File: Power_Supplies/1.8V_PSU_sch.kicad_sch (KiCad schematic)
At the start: 8 parts, among them U2 TPS62822DLC

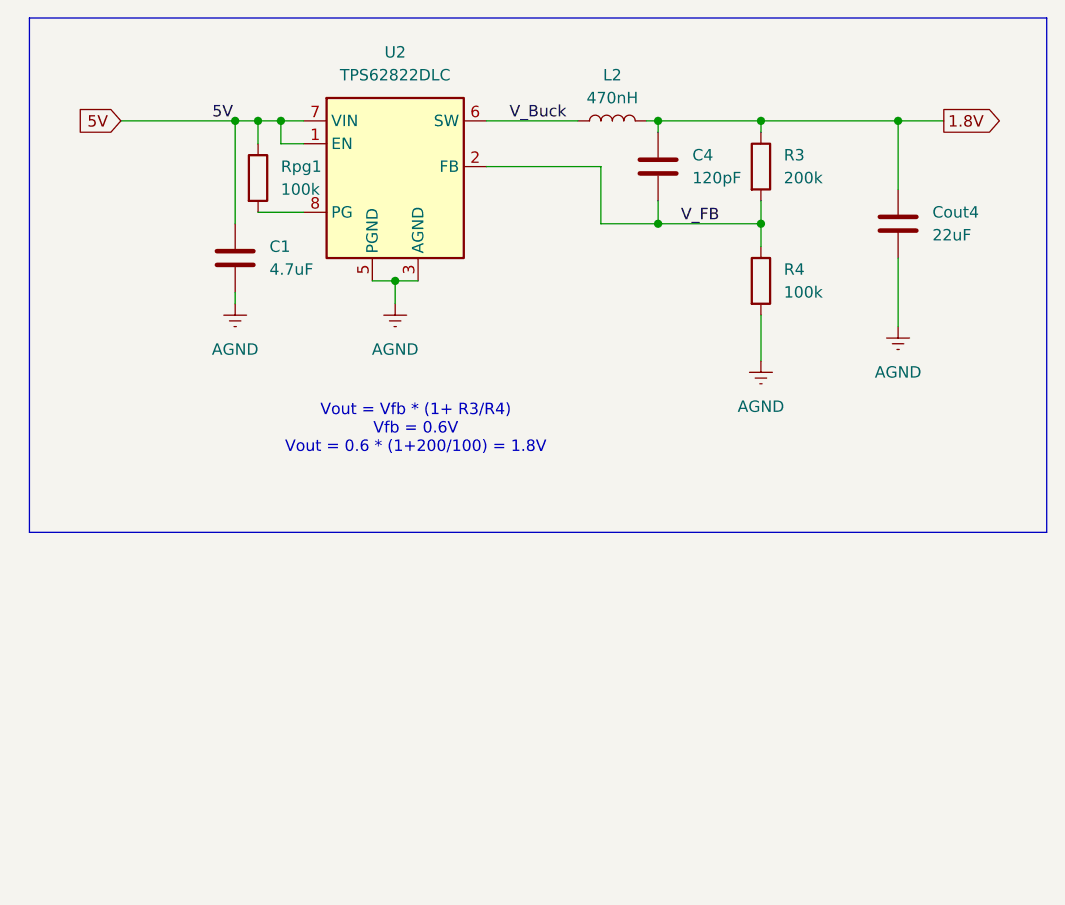
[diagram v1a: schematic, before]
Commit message: Added 3.3V/1.8V LDO, clock IC
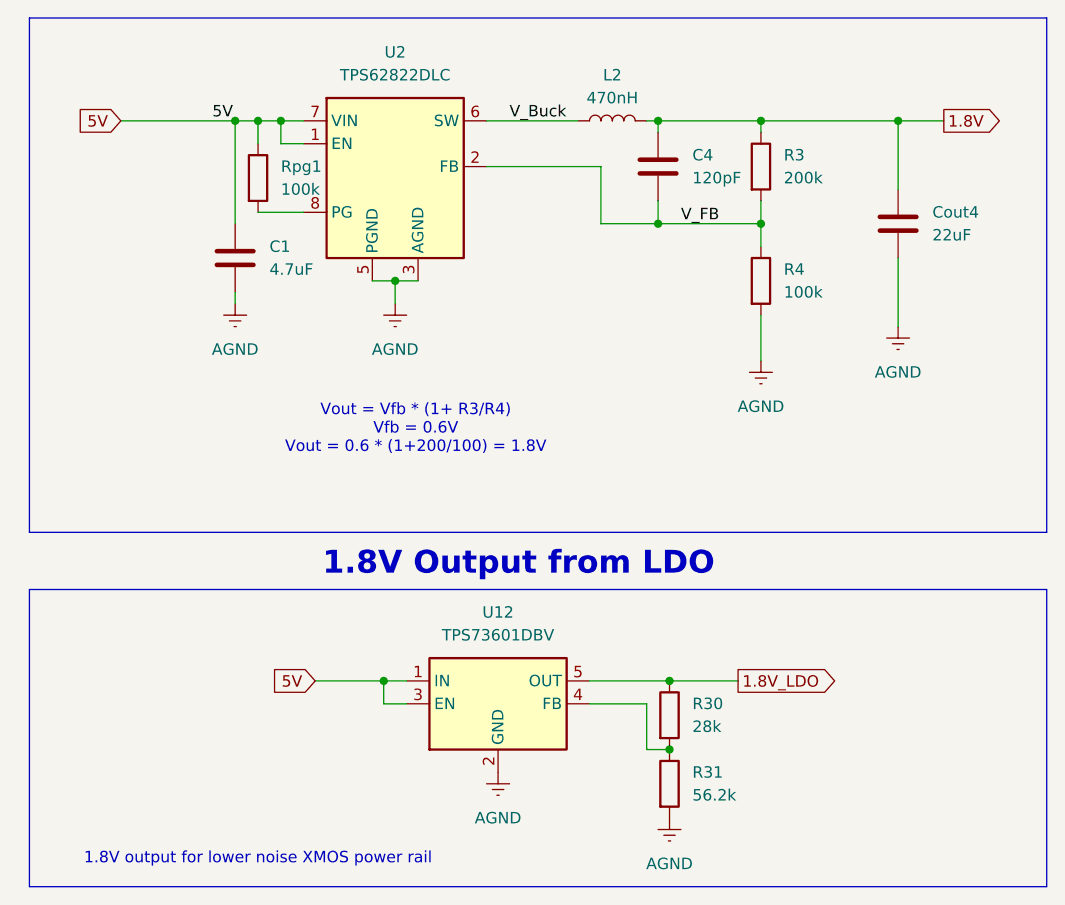
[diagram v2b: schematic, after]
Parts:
- added R30: 28k, Resistor_SMD:R_0805_2012Metric, symbol Device:R
- added R31: 56.2k, Resistor_SMD:R_0805_2012Metric, symbol Device:R
- added U12: TPS73601DBV, Package_TO_SOT_SMD:SOT-23-5, symbol Regulator_Linear:TPS73601DBV
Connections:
- net 5V: now also U12.1 (IN), U12.3 (EN)
- net AGND: now also R31.2, U12.2 (GND)
- new net: R30.2, R31.1, U12.4 (FB)
- new net 1.8V_LDO: R30.1, U12.5 (OUT)
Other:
- note added: "1.8V Output from LDO"
- note added: "1.8V output for lower noise XMOS power rail"
